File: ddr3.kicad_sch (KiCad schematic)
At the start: 2 parts, among them U1 MT41K256M16TW-107_P, U201 xc7z010clg400

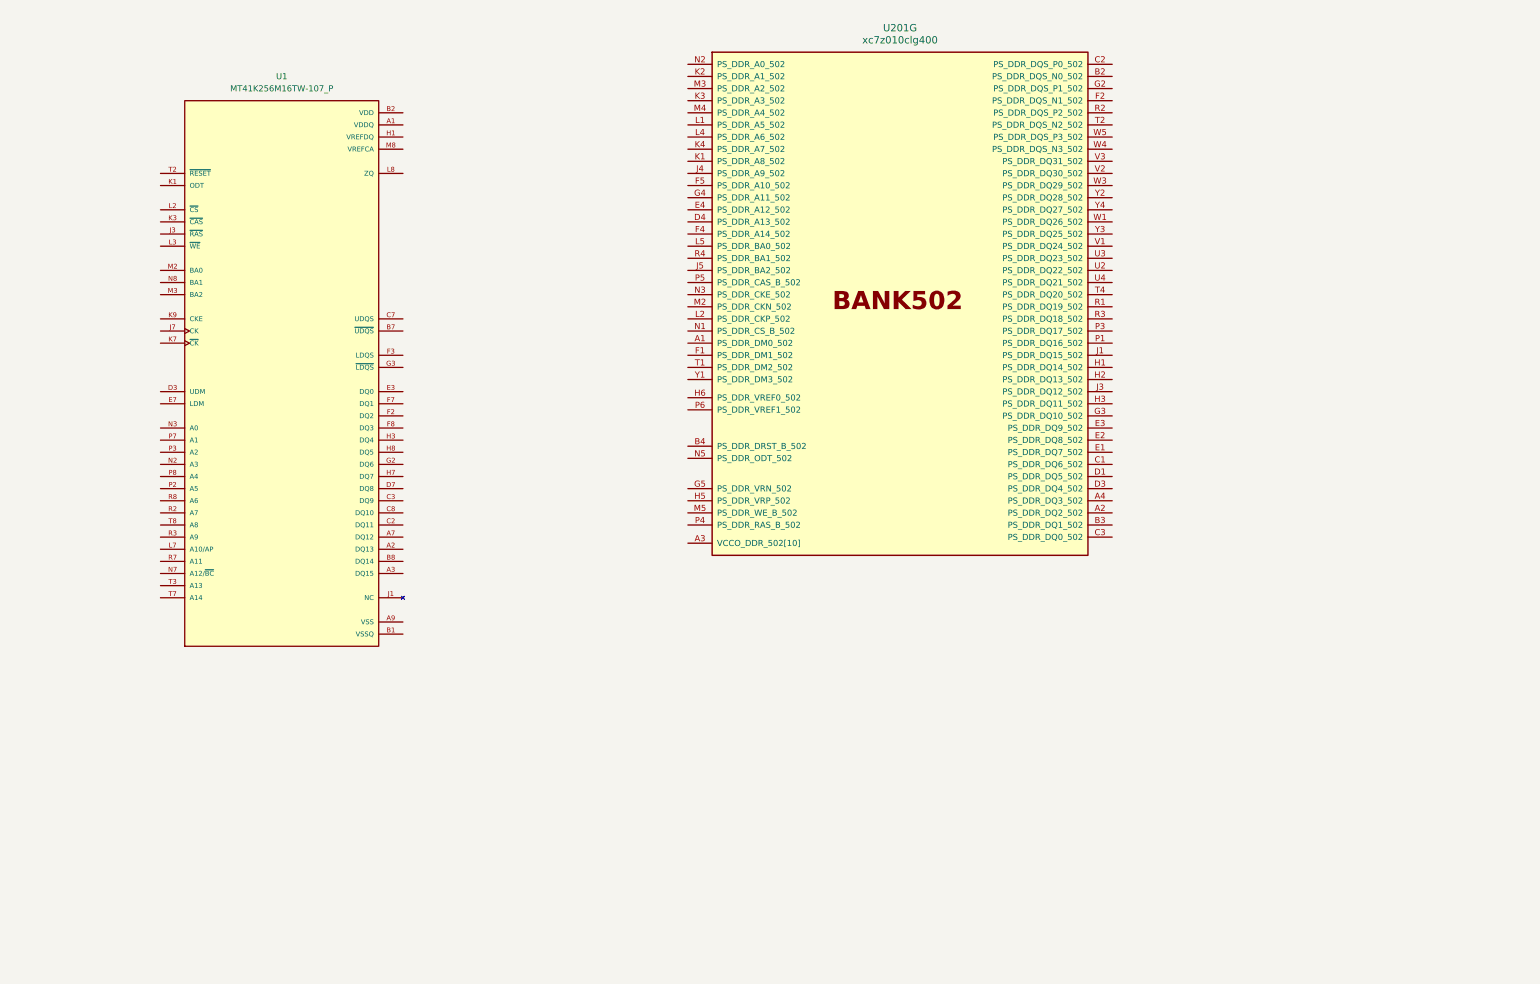
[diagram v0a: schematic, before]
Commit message: feat: finish ddr sch design
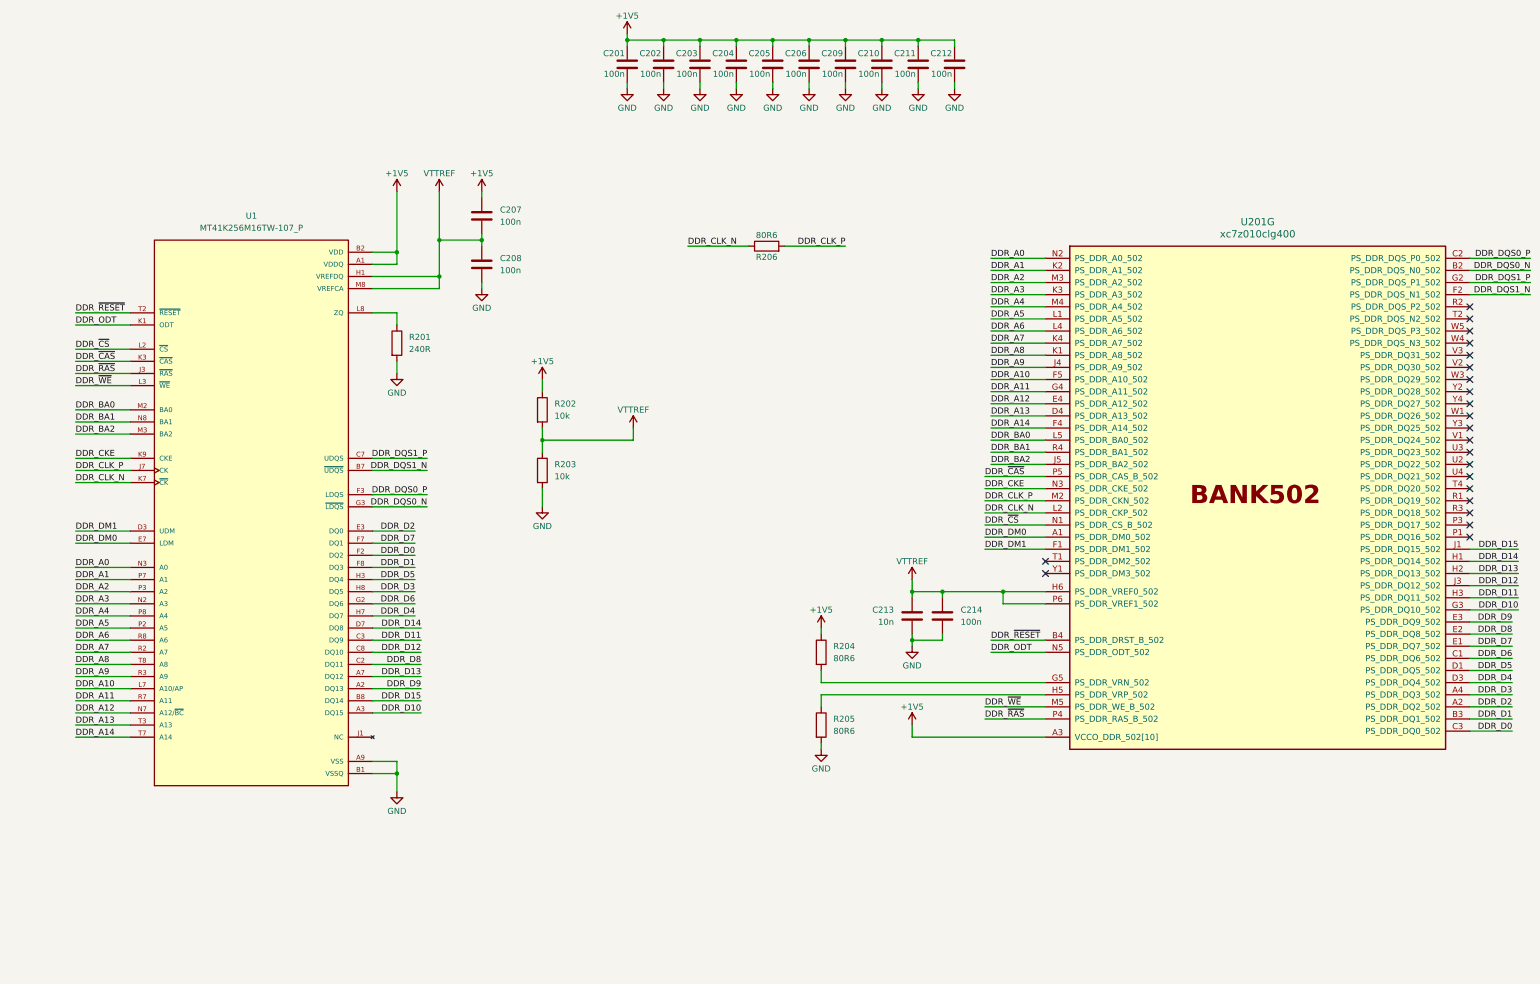
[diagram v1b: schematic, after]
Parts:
- added C201, C202, C203, C204, C205, C206, C207, C208, C209, C210, C211, C212, C214: 100n, Capacitor_SMD:C_0402_1005Metric, symbol Device:C
- added C213: 10n, Capacitor_SMD:C_0402_1005Metric, symbol Device:C
- added R201: 240R, Resistor_SMD:R_0402_1005Metric, symbol Device:R
- added R202, R203: 10k, Resistor_SMD:R_0402_1005Metric, symbol Device:R
- added R204, R205, R206: 80R6, Resistor_SMD:R_0402_1005Metric, symbol Device:R
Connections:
- net VDD is gone; now on net +1V5: U1.B2 (VDD), U1.D9 (VDD), U1.G7 (VDD), U1.K2 (VDD), U1.K8 (VDD), U1.N1 (VDD), U1.N9 (VDD), U1.R1 (VDD), U1.R9 (VDD)
- net VDDQ is gone; now on net +1V5: U1.A1 (VDDQ), U1.A8 (VDDQ), U1.C1 (VDDQ), U1.C9 (VDDQ), U1.D2 (VDDQ), U1.E9 (VDDQ), U1.F1 (VDDQ), U1.H2 (VDDQ), U1.H9 (VDDQ)
- net VSSQ is gone; now on net GND: U1.B1 (VSSQ), U1.B9 (VSSQ), U1.D1 (VSSQ), U1.D8 (VSSQ), U1.E2 (VSSQ), U1.E8 (VSSQ), U1.F9 (VSSQ), U1.G1 (VSSQ), U1.G9 (VSSQ)
- net DDR_DM0: now reaches U201.A1 (PS_DDR_DM0_502)
- net DDR_DM0: now also U1.E7 (LDM)
- net DDR_D2: now reaches U201.A2 (PS_DDR_DQ2_502)
- net DDR_D2: now also U1.E3 (DQ0)
- net +1V5: now reaches U201.A3 (VCCO_DDR_502[10]), U201.D2 (VCCO_DDR_502[10]), U201.E5 (VCCO_DDR_502[10]), U201.G1 (VCCO_DDR_502[10]), U201.H4 (VCCO_DDR_502[10]), U201.L3 (VCCO_DDR_502[10]), U201.P2 (VCCO_DDR_502[10]), U201.R5 (VCCO_DDR_502[10]), U201.U1 (VCCO_DDR_502[10]), U201.V4 (VCCO_DDR_502[10])
- net +1V5: now also C201.1, C202.1, C203.1, C204.1, C205.1, C206.1, C207.1, C209.1, C210.1, C211.1, C212.1, R202.1, R204.1
- net DDR_D3: now reaches U201.A4 (PS_DDR_DQ3_502)
- net DDR_D3: now also U1.H8 (DQ5)
- net DDR_DQS0_N: now reaches U201.B2 (PS_DDR_DQS_N0_502)
- net DDR_DQS0_N: now also U1.G3 (~{LDQS})
- net DDR_D1: now reaches U201.B3 (PS_DDR_DQ1_502)
- net DDR_D1: now also U1.F8 (DQ3)
- net DDR_~{RESET}: now reaches U201.B4 (PS_DDR_DRST_B_502)
- net DDR_~{RESET}: now also U1.T2 (~{RESET})
- net DDR_D6: now reaches U201.C1 (PS_DDR_DQ6_502)
- net DDR_D6: now also U1.G2 (DQ6)
- net DDR_DQS0_P: now reaches U201.C2 (PS_DDR_DQS_P0_502)
- net DDR_DQS0_P: now also U1.F3 (LDQS)
- net DDR_D0: now reaches U201.C3 (PS_DDR_DQ0_502)
- net DDR_D0: now also U1.F2 (DQ2)
- net DDR_D5: now reaches U201.D1 (PS_DDR_DQ5_502)
- net DDR_D5: now also U1.H3 (DQ4)
- net DDR_D4: now reaches U201.D3 (PS_DDR_DQ4_502)
- net DDR_D4: now also U1.H7 (DQ7)
- net DDR_A13: now reaches U201.D4 (PS_DDR_A13_502)
- net DDR_A13: now also U1.T3 (A13)
- net DDR_D7: now reaches U201.E1 (PS_DDR_DQ7_502)
- net DDR_D7: now also U1.F7 (DQ1)
- net DDR_D8: now reaches U201.E2 (PS_DDR_DQ8_502)
- net DDR_D8: now also U1.C2 (DQ11)
- net DDR_D9: now reaches U201.E3 (PS_DDR_DQ9_502)
- net DDR_D9: now also U1.A2 (DQ13)
- net DDR_A12: now reaches U201.E4 (PS_DDR_A12_502)
- net DDR_A12: now also U1.N7 (A12/~{BC})
- net DDR_DM1: now reaches U201.F1 (PS_DDR_DM1_502)
- net DDR_DM1: now also U1.D3 (UDM)
- net DDR_DQS1_N: now reaches U201.F2 (PS_DDR_DQS_N1_502)
- net DDR_DQS1_N: now also U1.B7 (~{UDQS})
- net DDR_A14: now reaches U201.F4 (PS_DDR_A14_502)
- net DDR_A14: now also U1.T7 (A14)
- net DDR_A10: now reaches U201.F5 (PS_DDR_A10_502)
- net DDR_A10: now also U1.L7 (A10/AP)
- net DDR_DQS1_P: now reaches U201.G2 (PS_DDR_DQS_P1_502)
- net DDR_DQS1_P: now also U1.C7 (UDQS)
- net DDR_D10: now reaches U201.G3 (PS_DDR_DQ10_502)
- net DDR_D10: now also U1.A3 (DQ15)
- net DDR_A11: now reaches U201.G4 (PS_DDR_A11_502)
- net DDR_A11: now also U1.R7 (A11)
- net at U201.G5 (PS_DDR_VRN_502): now also R204.2
- net DDR_D14: now reaches U201.H1 (PS_DDR_DQ14_502)
- net DDR_D14: now also U1.D7 (DQ8)
- net DDR_D13: now reaches U201.H2 (PS_DDR_DQ13_502)
- net DDR_D13: now also U1.A7 (DQ12)
- net DDR_D11: now reaches U201.H3 (PS_DDR_DQ11_502)
- net DDR_D11: now also U1.C3 (DQ9)
- net at U201.H5 (PS_DDR_VRP_502): now also R205.1
- net VTTREF: now reaches U201.H6 (PS_DDR_VREF0_502)
- net VTTREF: now also U1.H1 (VREFDQ), U1.M8 (VREFCA), U201.P6 (PS_DDR_VREF1_502), C207.2, C208.1, C213.1, C214.1, R202.2, R203.1
- net DDR_D15: now reaches U201.J1 (PS_DDR_DQ15_502)
- net DDR_D15: now also U1.B8 (DQ14)
- net DDR_D12: now reaches U201.J3 (PS_DDR_DQ12_502)
- net DDR_D12: now also U1.C8 (DQ10)
- net DDR_A9: now reaches U201.J4 (PS_DDR_A9_502)
- net DDR_A9: now also U1.R3 (A9)
- net DDR_BA2: now reaches U201.J5 (PS_DDR_BA2_502)
- net DDR_BA2: now also U1.M3 (BA2)
- net DDR_A8: now reaches U201.K1 (PS_DDR_A8_502)
- net DDR_A8: now also U1.T8 (A8)
- net DDR_A1: now reaches U201.K2 (PS_DDR_A1_502)
- net DDR_A1: now also U1.P7 (A1)
- net DDR_A3: now reaches U201.K3 (PS_DDR_A3_502)
- net DDR_A3: now also U1.N2 (A3)
- net DDR_A7: now reaches U201.K4 (PS_DDR_A7_502)
- net DDR_A7: now also U1.R2 (A7)
- net DDR_A5: now reaches U201.L1 (PS_DDR_A5_502)
- net DDR_A5: now also U1.P2 (A5)
- net DDR_CLK_N: now reaches U201.L2 (PS_DDR_CKP_502)
- net DDR_CLK_N: now also U1.K7 (~{CK}), R206.1
- net DDR_A6: now reaches U201.L4 (PS_DDR_A6_502)
- net DDR_A6: now also U1.R8 (A6)
- net DDR_BA0: now reaches U201.L5 (PS_DDR_BA0_502)
- net DDR_BA0: now also U1.M2 (BA0)
- net DDR_CLK_P: now reaches U201.M2 (PS_DDR_CKN_502)
- net DDR_CLK_P: now also U1.J7 (CK), R206.2
- net DDR_A2: now reaches U201.M3 (PS_DDR_A2_502)
- net DDR_A2: now also U1.P3 (A2)
- net DDR_A4: now reaches U201.M4 (PS_DDR_A4_502)
- net DDR_A4: now also U1.P8 (A4)
- net DDR_~{WE}: now reaches U201.M5 (PS_DDR_WE_B_502)
- net DDR_~{WE}: now also U1.L3 (~{WE})
- net DDR_~{CS}: now reaches U201.N1 (PS_DDR_CS_B_502)
- net DDR_~{CS}: now also U1.L2 (~{CS})
- net DDR_A0: now reaches U201.N2 (PS_DDR_A0_502)
- net DDR_A0: now also U1.N3 (A0)
- net DDR_CKE: now reaches U201.N3 (PS_DDR_CKE_502)
- net DDR_CKE: now also U1.K9 (CKE)
- net DDR_ODT: now reaches U201.N5 (PS_DDR_ODT_502)
- net DDR_ODT: now also U1.K1 (ODT)
- net DDR_~{RAS}: now reaches U201.P4 (PS_DDR_RAS_B_502)
- net DDR_~{RAS}: now also U1.J3 (~{RAS})
- net DDR_~{CAS}: now reaches U201.P5 (PS_DDR_CAS_B_502)
- net DDR_~{CAS}: now also U1.K3 (~{CAS})
- net DDR_BA1: now reaches U201.R4 (PS_DDR_BA1_502)
- net DDR_BA1: now also U1.N8 (BA1)
- net at U1.L8 (ZQ): now also R201.1
- net VSS renamed GND
- net GND: now also C201.2, C202.2, C203.2, C204.2, C205.2, C206.2, C208.2, C209.2, C210.2, C211.2, C212.2, C213.2, C214.2, R201.2, R203.2, R205.2
- no-connect marks 0 -> 22
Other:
- moved on the sheet: U1, U201G

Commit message: feat: finish power sch design
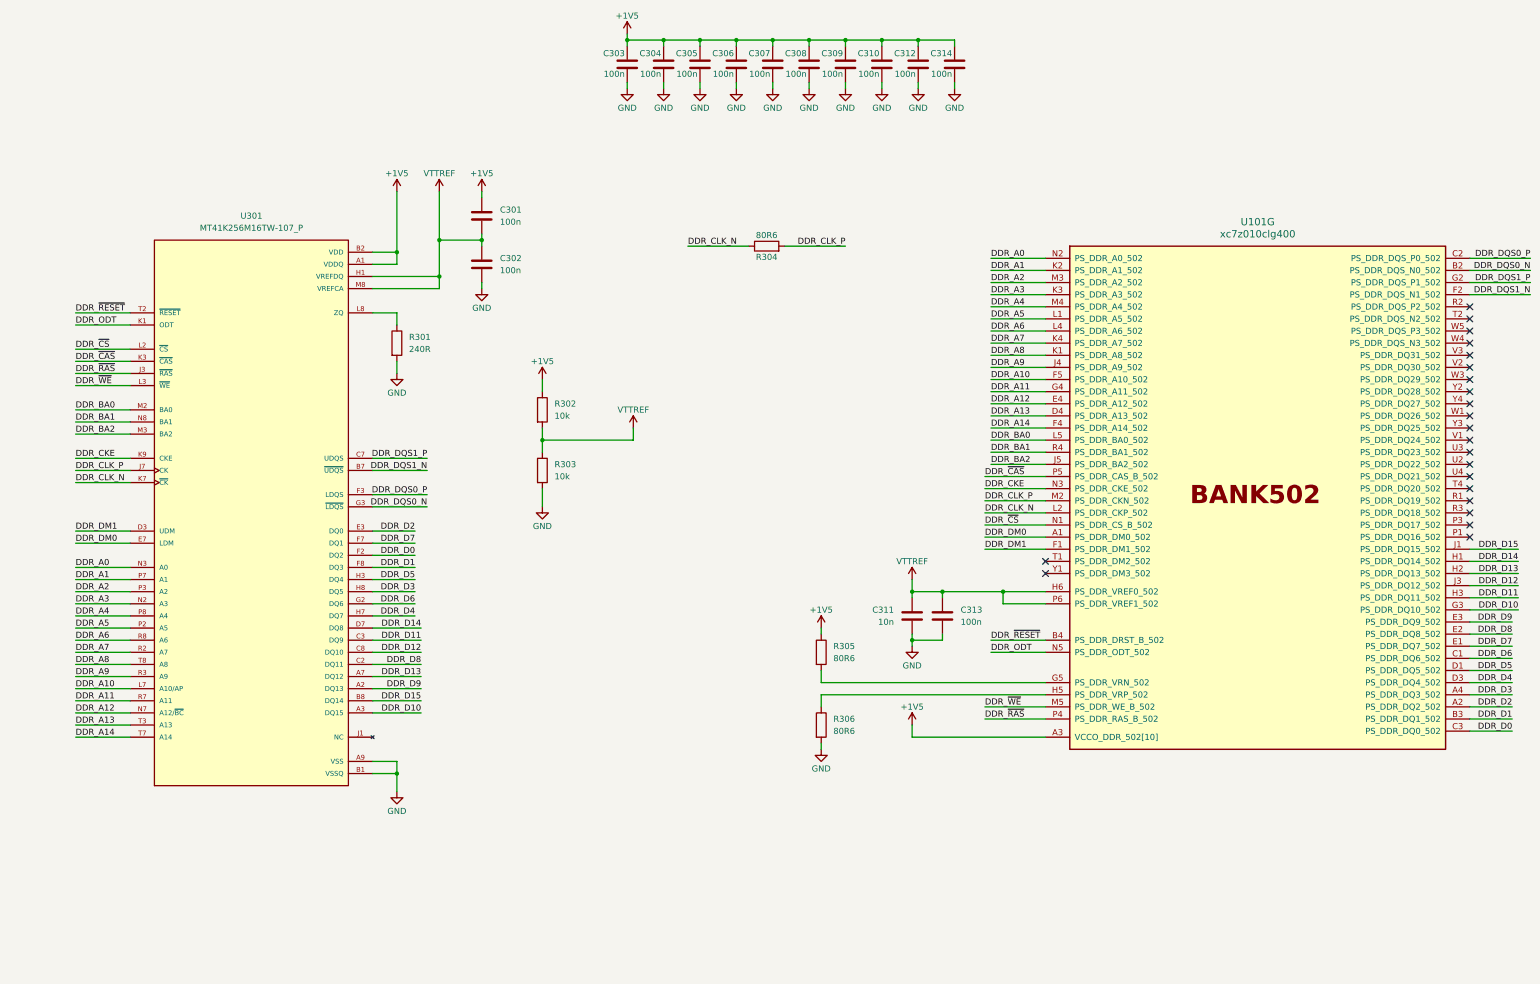
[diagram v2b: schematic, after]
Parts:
- renumbered C207 to C301, C208 to C302, C201 to C303, C202 to C304, C203 to C305, C204 to C306, C205 to C307, C206 to C308, C209 to C309, C210 to C310, C213 to C311, C211 to C312, C214 to C313, C212 to C314, R201 to R301, R202 to R302, R203 to R303, R206 to R304, R204 to R305, R205 to R306, U201 to U101, U1 to U301

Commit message: feat: continue ps mio sch design
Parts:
- renumbered U101 to U201
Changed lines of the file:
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@@
 		(dnp no)
 		(fields_autoplaced yes)
-		(property "Reference" "U101"
+		(property "Reference" "U201"
 			(at 293.37 67.31 0)
 			(show_name no)
@@
 			(project "ZYNQ-SoM"
 				(path "/49bbd0e9-23a3-4368-9660-7ba6c337a59d/947e469f-e1e3-460e-9031-ccc4285a0168"
-					(reference "U101")
+					(reference "U201")
 					(unit 7)
 				)

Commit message: feat: continue improve sch design
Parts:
- removed R303: 10k, Resistor_SMD:R_0402_1005Metric, symbol Device:R
- added C315: 10u, Capacitor_SMD:C_0805_2012Metric, symbol Device:C
- added C317, C321, C322: 100n, Capacitor_SMD:C_0402_1005Metric, symbol Device:C
- added R307, R308, R309, R310, R311, R312, R313, R314, R315, R316, R317, R318, R319, R320, R321, R322, R323, R324, R325, R326, R327, R328, R329, R330: 40R2, Resistor_SMD:R_0402_1005Metric, symbol Device:R
- R302: value 10k -> 4k7
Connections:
- net +1V5: no longer R302.1
- net DDR_A0: now also R307.1
- net DDR_A1: now also R308.1
- net DDR_A10: now also R317.1
- net DDR_A11: now also R318.1
- net DDR_A12: now also R319.1
- net DDR_A13: now also R320.1
- net DDR_A14: now also R321.1
- net DDR_A2: now also R309.1
- net DDR_A3: now also R310.1
- net DDR_A4: now also R311.1
- net DDR_A5: now also R312.1
- net DDR_A6: now also R313.1
- net DDR_A7: now also R314.1
- net DDR_A8: now also R315.1
- net DDR_A9: now also R316.1
- net DDR_BA0: now also R322.1
- net DDR_BA1: now also R323.1
- net DDR_BA2: now also R324.1
- net DDR_CKE: now also R330.1
- net DDR_ODT: now also R326.1
- net DDR_~{CAS}: now also R329.1
- net DDR_~{CS}: now also R325.1
- net DDR_~{RAS}: now also R328.1
- net DDR_~{RESET}: now also R302.1
- net DDR_~{WE}: now also R327.1
- net GND: now also R302.2, C315.2, C317.2, C321.2, C322.2
- net VTTREF: no longer C301.2, C302.1, R302.2, U301.H1 (VREFDQ), U301.M8 (VREFCA)
- new net +DDRVTT: C315.1, C317.1, C321.1, C322.1, R307.2, R308.2, R309.2, R310.2, R311.2, R312.2, R313.2, R314.2, R315.2, R316.2, R317.2, R318.2, R319.2, R320.2, R321.2, R322.2, R323.2, R324.2, R325.2, R326.2, R327.2, R328.2, R329.2, R330.2
- new net +VTTREF: C301.2, C302.1, U301.H1 (VREFDQ), U301.M8 (VREFCA)
